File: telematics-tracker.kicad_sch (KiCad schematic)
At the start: 0 parts

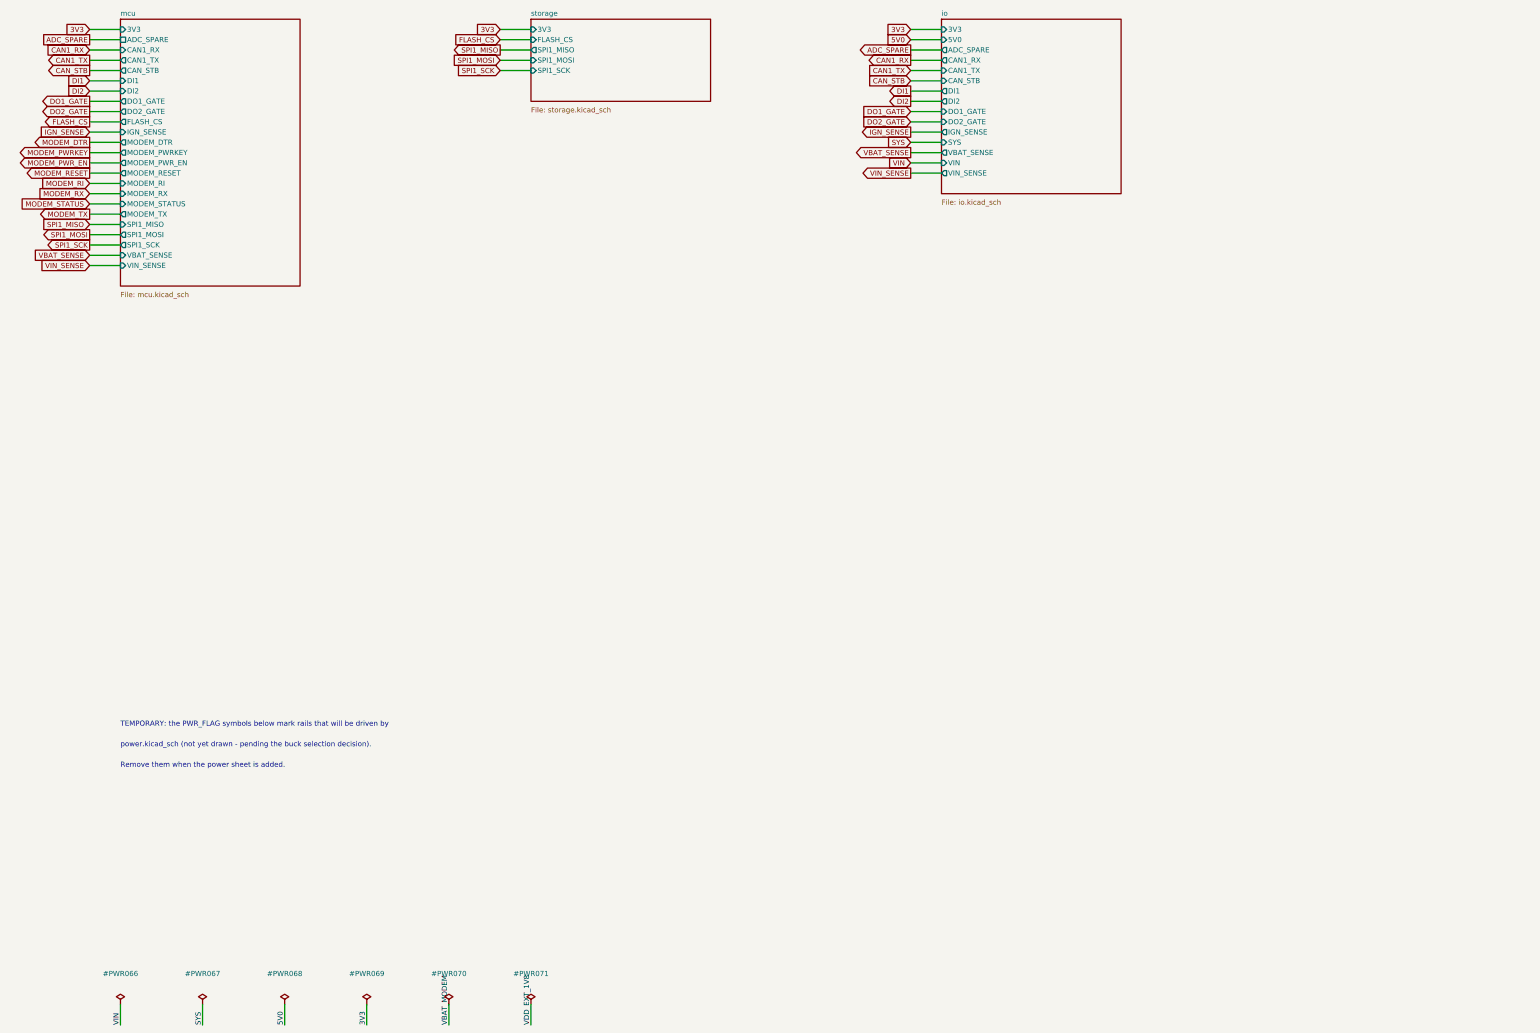
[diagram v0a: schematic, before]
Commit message: M2: modem_rf ERC-clean (F-9 conditional release)
EC200U wired using ONLY Table-7-VERIFIED pins; all 76 NEEDS-HUMAN pins are
no-connect with F9-REVIEW text markers on the sheet. VBAT (57-60) via Q3
AO3401A high-side switch (DEFAULT ON, MODEM_PWR_EN high = power cut via
Q14 NPN + Q13 PNP); PWRKEY/RESET_N NPN open-collector stages; STATUS per
Quectel Fig 28 NPN stage (MODEM_STATUS INVERTED at MCU - firmware note);
UART/RI/DTR through TXB0104PWR (VccA=VDD_EXT 1.8V, OE held low until
VDD_EXT rises); USIM with 33R series + SMF05C + nano holder + MFF2 eSIM
pads DNP behind 0R selects; USB to 4 test pads via USBLC6-2SC6; NETLIGHT
NPN LED; pi networks (0R fitted, shunts DNP) to 2x XY-IPEX1 U.FL.

Root-sheet layout bug fixed: a 5th sheet wrapped onto column 0 and its
pin stubs shorted into the mcu sheet's stubs (5V0/ADC_SPARE, CAN1_RX/SYS,
CAN1_TX/VIN) - rows added. USIM_VDD 0R select was defeated by a label
bridge - holder now on USIM_VDD_SIM only.

Co-Authored-By: Claude Fable 5 <noreply@anthropic.com>
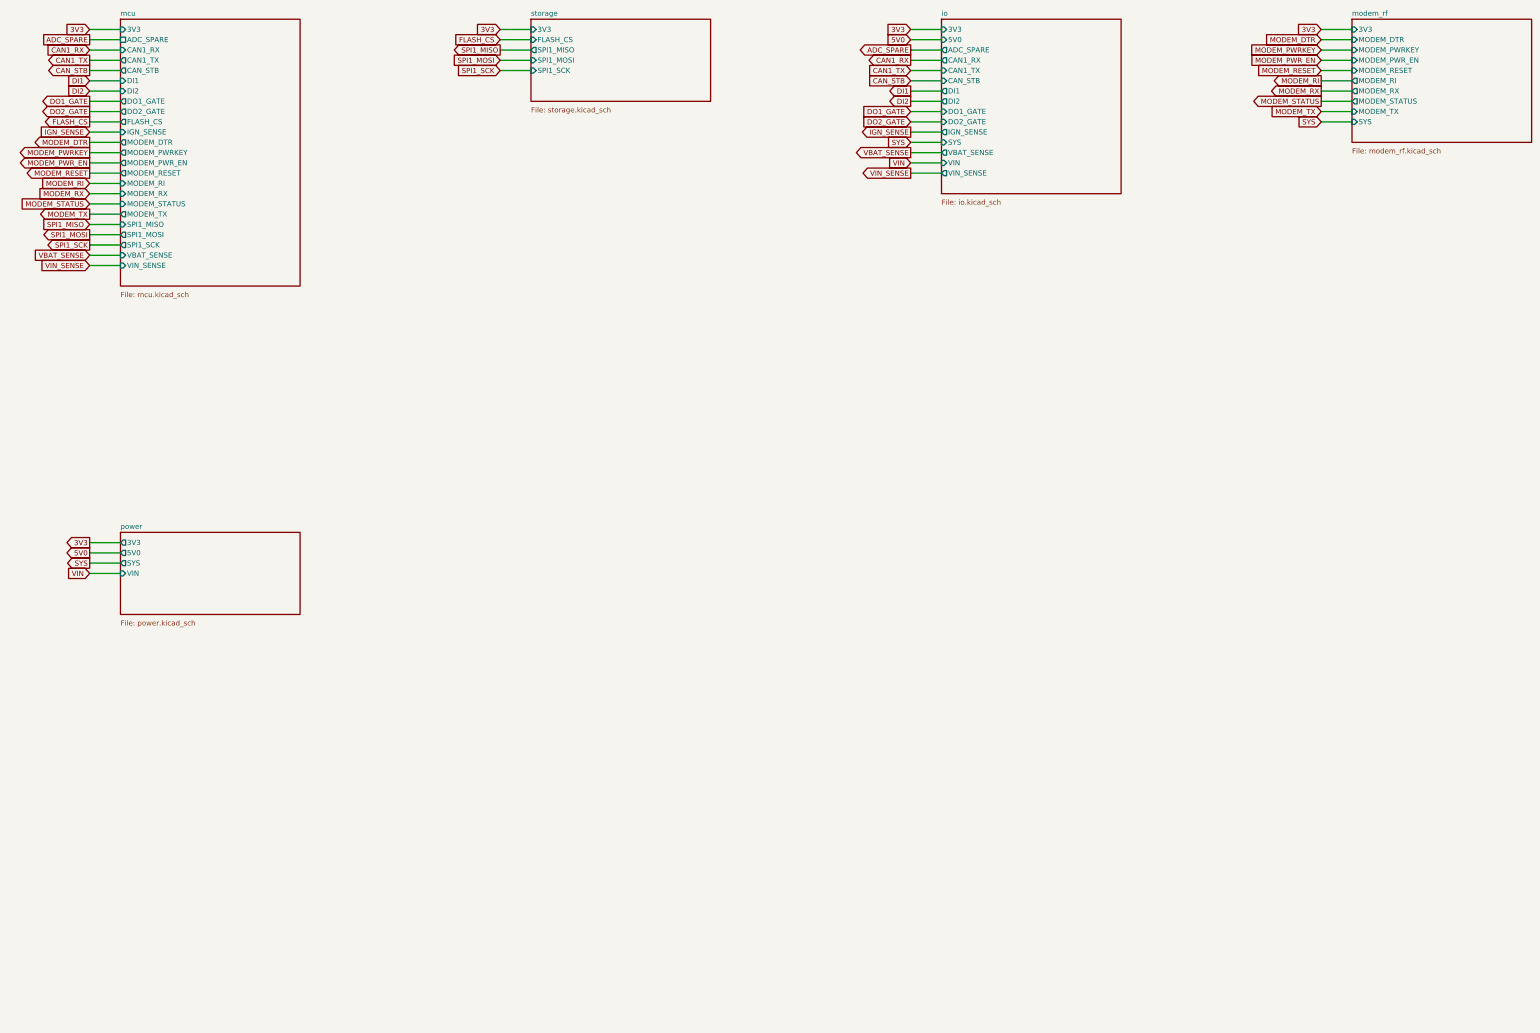
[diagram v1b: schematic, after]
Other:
- added sheet modem_rf (modem_rf.kicad_sch)
- added sheet power (power.kicad_sch)
- note removed: "Remove them when the power sheet is added."
- note removed: "TEMPORARY: the PWR_FLAG symbols below mark rails that will be driven by"
- note removed: "power.kicad_sch (not yet drawn - pending the buck selection decision)."

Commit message: Step 1-3: fix rule floors, classify SW_BUCK as HV, shrink, fix HV router
Step 1 - rule mismatch fixed and verified:
  netclasses.py gains BOARD_RULES + _assert_floors(). Every class now meets
  track >= 0.20 mm and via annulus >= 0.10 mm. min_clearance had been silently
  reset to 0.0 by a KiCad round trip; restored to 0.15 and now asserted after
  the round trip so it cannot regress unnoticed. Exported DSN verified to carry
  the values (kicad_default 200, GND 500, MODEM_BULK 2000, RF 400, HV 500/600).

Step 2 - HV hand-routing, and three real defects it uncovered:

  1. /power/SW_BUCK was in the Default netclass. It is the buck switching node:
     it swings from GND to VIN every cycle, so it is a 100 V net with fast
     edges, and it was running at 0.20 mm track / 0.15 mm clearance. U5_VB
     (bootstrap) rides on it and was equally misclassified. Both moved to HV.
     Found because the maze router treated SW_BUCK as LV and threw a 1.50 mm
     halo around U5's own VIN pins, making /power/VIN_B unroutable at 0/4.

  2. HV_ZONE stopped at x = 20.0 and so EXCLUDED the buck primary side. U5 sits
     at x 35.4..42.3 with C73, C74 and D16 beside it, and VIN_B runs 22 mm from
     R80 to reach it. The highest-energy node on the board was outside the HV
     rule area - which also meant the U5 package exception approved under F-20
     was dead code, since it is conditioned on insideArea('HV_ZONE'). HV_ZONE
     is now L-shaped: left strip plus the buck primary.

  3. Three defects in pcbroute_hv.py itself, together responsible for 128 of
     the 129 clearance violations the first routed board had:
       - halos were sized for a 0.50 mm track (half 0.25) but the router also
         drops 0.80 mm vias, so cells legal for a track were illegal for a via
       - halo extents were quantised with round(), letting a cell centre sit up
         to RES/2 = 0.075 mm inside the forbidden region. That is exactly the
         size of the 0.545..0.594 mm shortfalls DRC reporte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
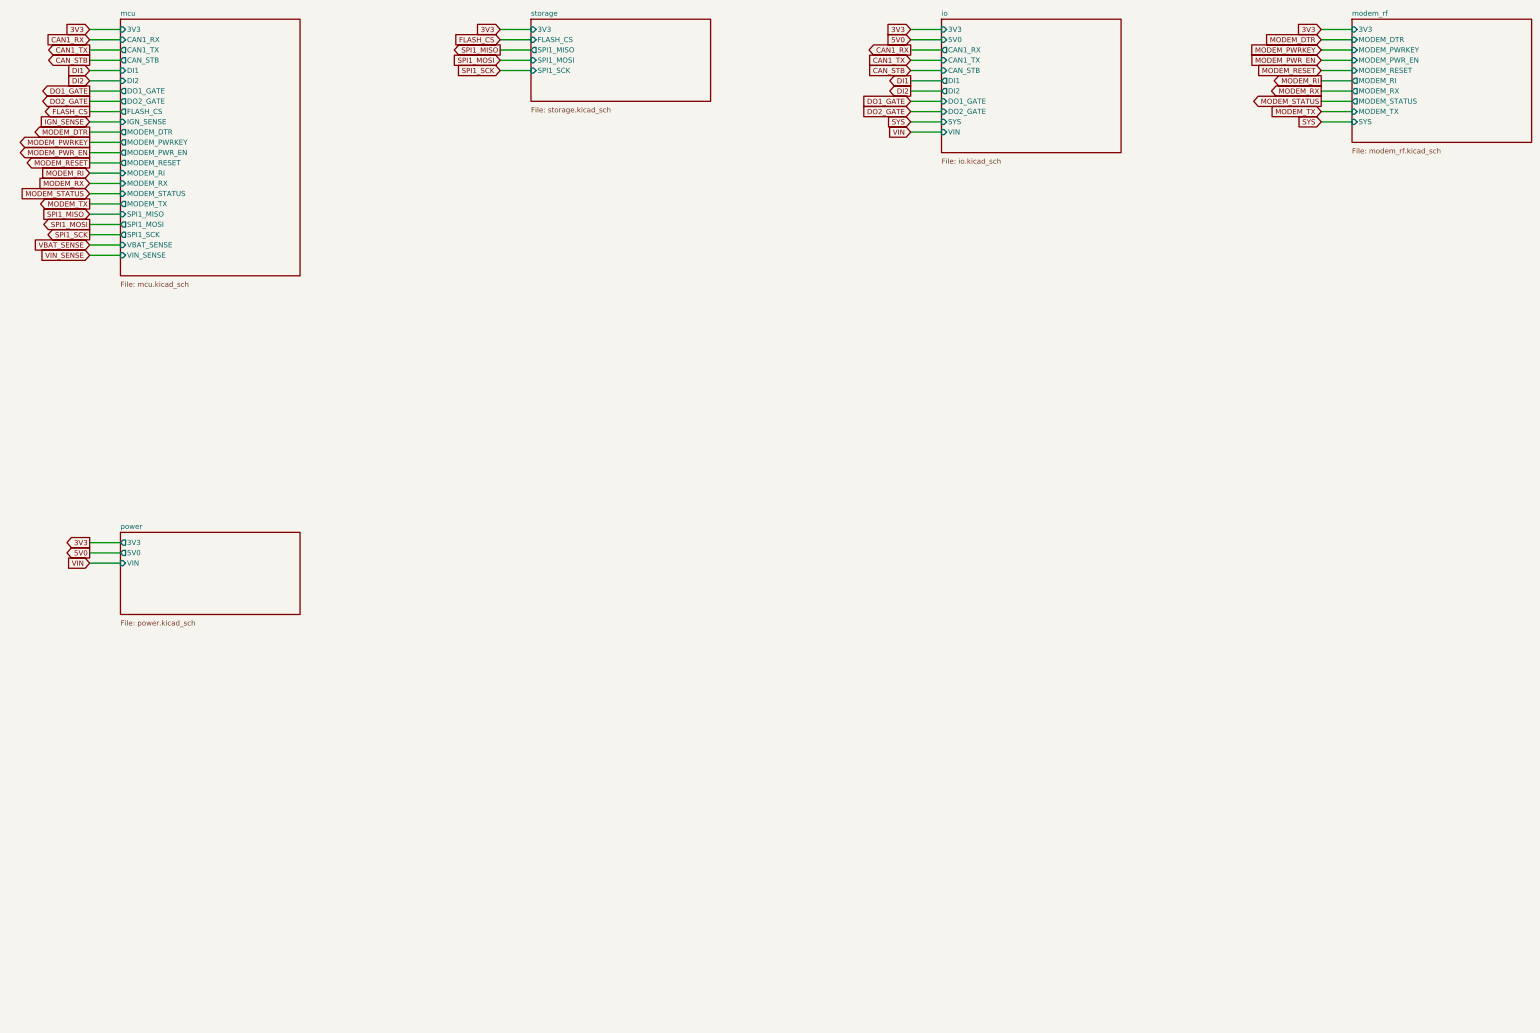
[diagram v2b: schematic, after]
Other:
- sheet io ports: added none; removed ADC_SPARE, IGN_SENSE, VBAT_SENSE, VIN_SENSE
- sheet mcu ports: added none; removed ADC_SPARE
- sheet power ports: added none; removed SYS

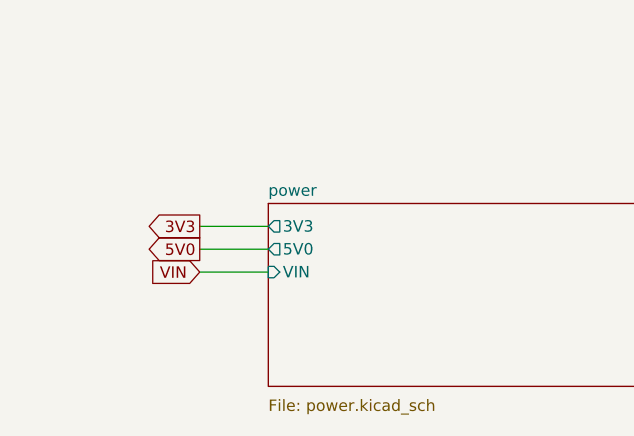
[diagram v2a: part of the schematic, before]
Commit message: Fix split SYS rail; relief round 3 anchors; L3 pours redrawn to the pads
SCHEMATIC FAULT FIXED: the power sheet carried only LOCAL "SYS" labels, so
the charger output (U6.15/16, L3, C65/C66/C68, U9 input) was net /power/SYS
and never left the sheet, while the modem power switch (Q3, Q13, R52), the
battery-sense divider (R38) and TP13 sat on a global SYS with no source.
ERC reported it only as same_local_global_label (a "justified" warning).
U6.15 now carries a hierarchical label like 3V3/5V0 do; SYS is one net of
11 members. ERC 0 errors / 22 warnings (same two benign classes);
checkpins 48/48 still passes.

Placement (relief round 3, variant A of four parallel trials): U8 -> back
side (49.9, 47.0) beside X1/U1, its only partners; U7 -> back side
(46.9, 15.6), out of U2's west escape corridor. Variant A reached 92
unconnected after one hybrid cycle from a fresh regeneration (floor was 109).

L3 pours: measured on the routed board, the old "5V0" band y 27.5-39 held
14 3V3 pads and 4 5V0 pads, the "SYS" band held 5 of the 5V0 pads, and the
north "3V3 finger" held no 3V3 pad - so pour-taps were impossible for most
power pads. 3V3 is now the background pour of the LV area; 5V0 and SYS get
tight priority-1 islands computed by a greedy no-foreign-pad search
(13/16 5V0 pads, 9/13 SYS pads covered; no 3V3 pad lands in a foreign
island). VBAT_MODEM keeps its island at priority 1.

Co-Authored-By: Claude Fable 5.1 <noreply@anthropic.com>
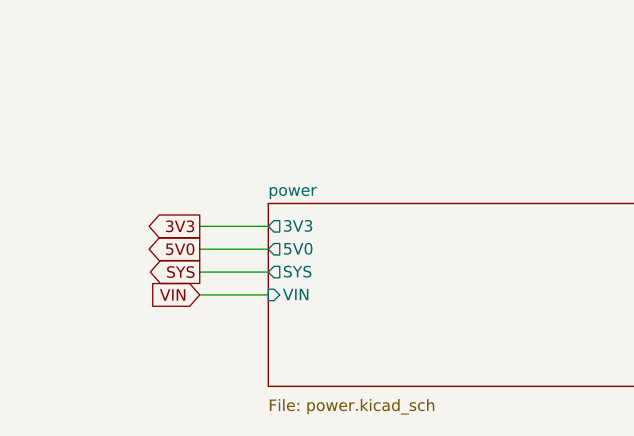
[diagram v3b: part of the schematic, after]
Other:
- sheet power ports: added SYS; removed none
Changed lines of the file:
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@@
 		)
 	)
-	(global_label "VIN"
-		(shape input)
+	(global_label "SYS"
+		(shape output)
 		(at 17.78 160.02 180)
 		(fields_autoplaced yes)
@@
 		(property "Intersheetrefs" "${INTERSHEET_REFS}"
 			(at 17.78 160.02 0)
+			(hide yes)
+			(effects
+				(font
+					(size 1.27 1.27)
+				)
+				(justify right)
+			)
+		)
+	)
+	(wire
+		(pts
+			(xy 25.4 162.56) (xy 17.78 162.56)
+		)
+		(stroke
+			(width 0)
+			(type default)
+		)
+	)
+	(global_label "VIN"
+		(shape input)
+		(at 17.78 162.56 180)
+		(fields_autoplaced yes)
+		(effects
+			(font
+				(size 1.27 1.27)
+			)
+			(justify right)
+		)
+		(property "Intersheetrefs" "${INTERSHEET_REFS}"
+			(at 17.78 162.56 0)
 			(hide yes)
 			(effects
@@
 			)
 		)
+		(pin "SYS" output
+			(at 25.4 160.02 180)
+			(effects
+				(font
+					(size 1.27 1.27)
+				)
+				(justify right)
+			)
+		)
 		(pin "VIN" input
-			(at 25.4 160.02 180)
-			(effects
-				(font
+			(at 25.4 162.56 180)
+			(effects
+				(font
